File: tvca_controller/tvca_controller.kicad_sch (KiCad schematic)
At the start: 17 parts, among them J1 Programming Header, J2 Can Connector, U1 MCP2562, U2 PIC18F26K83, U5 INA180A1, Y1 Crystal

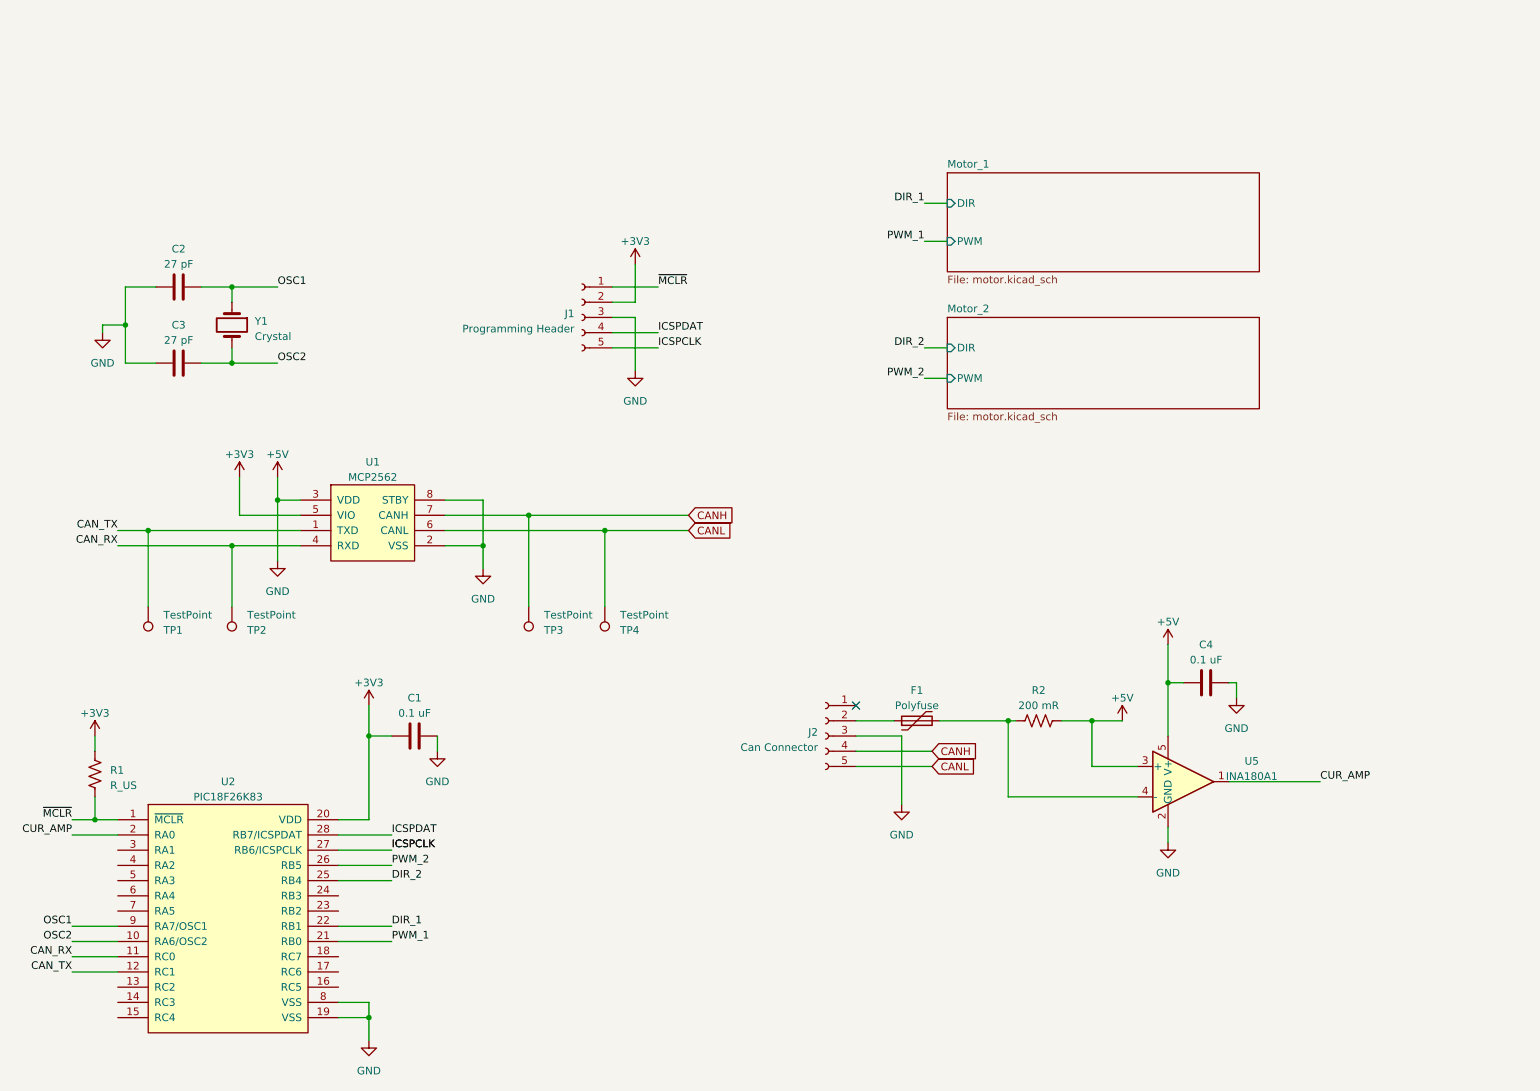
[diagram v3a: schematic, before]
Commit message: remove zips, refactor PCB to use software in place of 2-bit mux
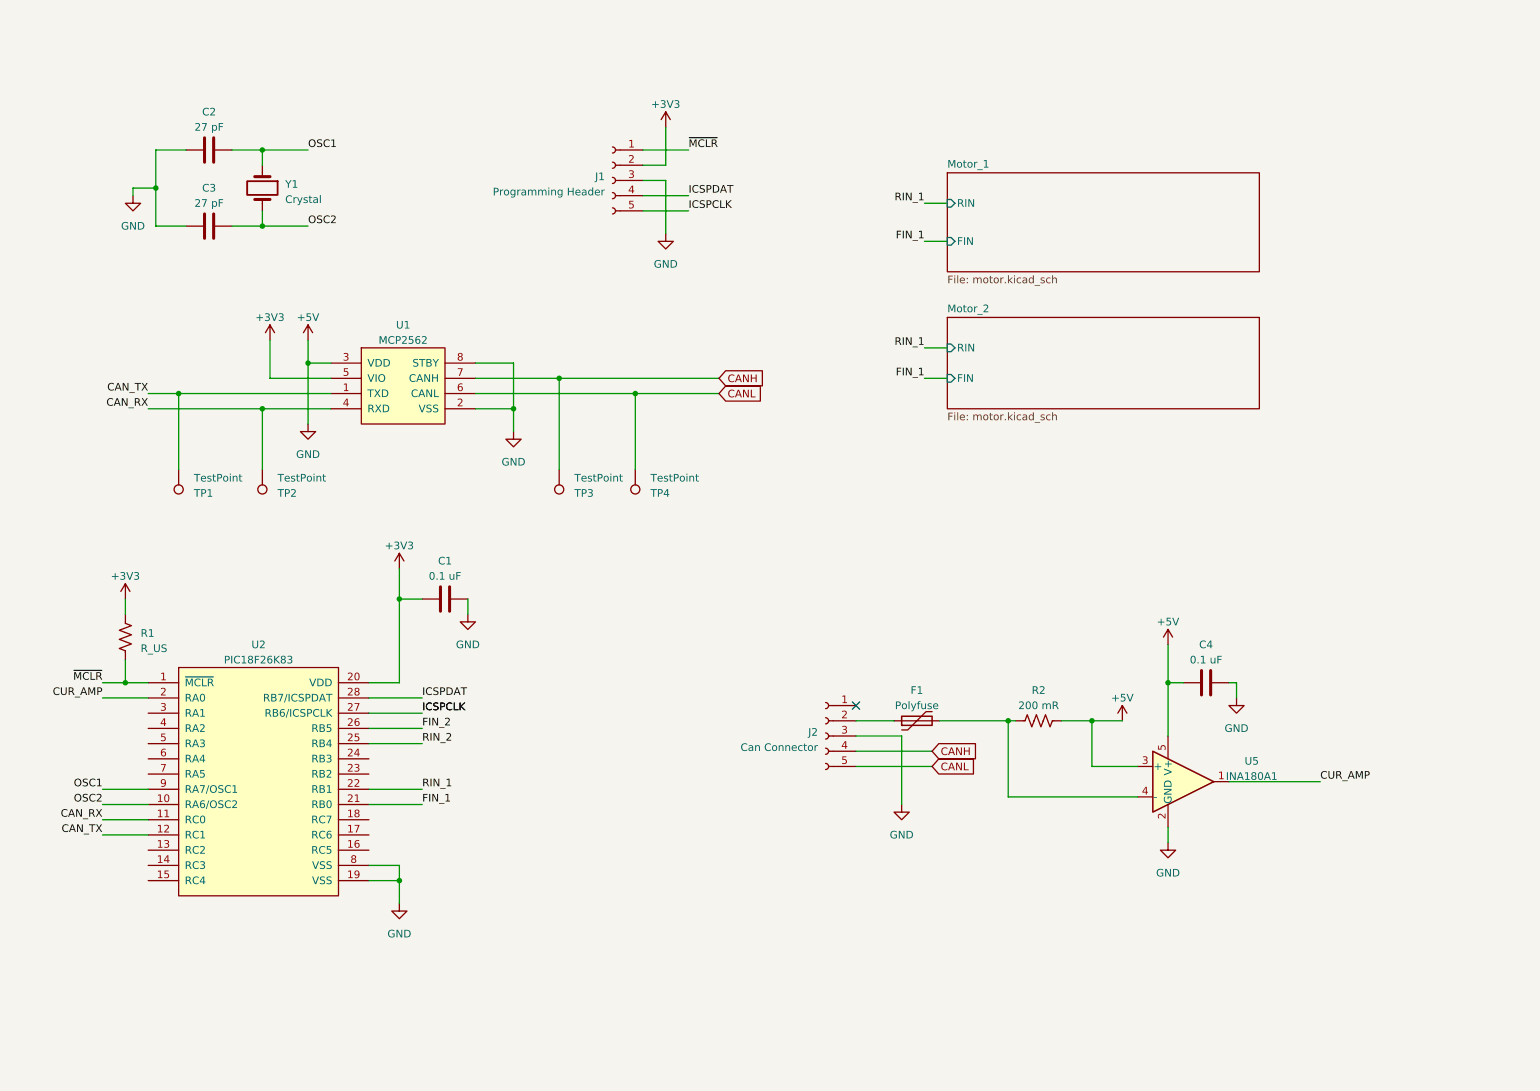
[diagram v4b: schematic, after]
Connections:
- net DIR_1 renamed RIN_1
- net DIR_2 renamed RIN_2
- net PWM_1 renamed FIN_1
- net PWM_2 renamed FIN_2
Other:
- sheet Motor_1 ports: added FIN, RIN; removed DIR, PWM
- sheet Motor_2 ports: added FIN, RIN; removed DIR, PWM
- moved on the sheet: C1, C2, C3, J1, R1, TP1, TP2, TP3, TP4, U1, U2, Y1

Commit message: add connectors
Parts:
- added J7: Batt - 12V, symbol Connector:Screw_Terminal_01x02
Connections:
- net +5V: now also J7.2 (Pin_2)
- net A_1: now reaches U2.3 (RA1)
- net B_1: now reaches U2.4 (RA2)
- net A_2: now reaches U2.5 (RA3)
- net B_2: now reaches U2.6 (RA4)
- new net BATT: J7.1 (Pin_1)
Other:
- sheet Motor_1 ports: added A, B, POW; removed none
- sheet Motor_2 ports: added A, B, POW; removed none
- note added: "PWM Input Signals"
- note added: "Quadrature Encoder Output"

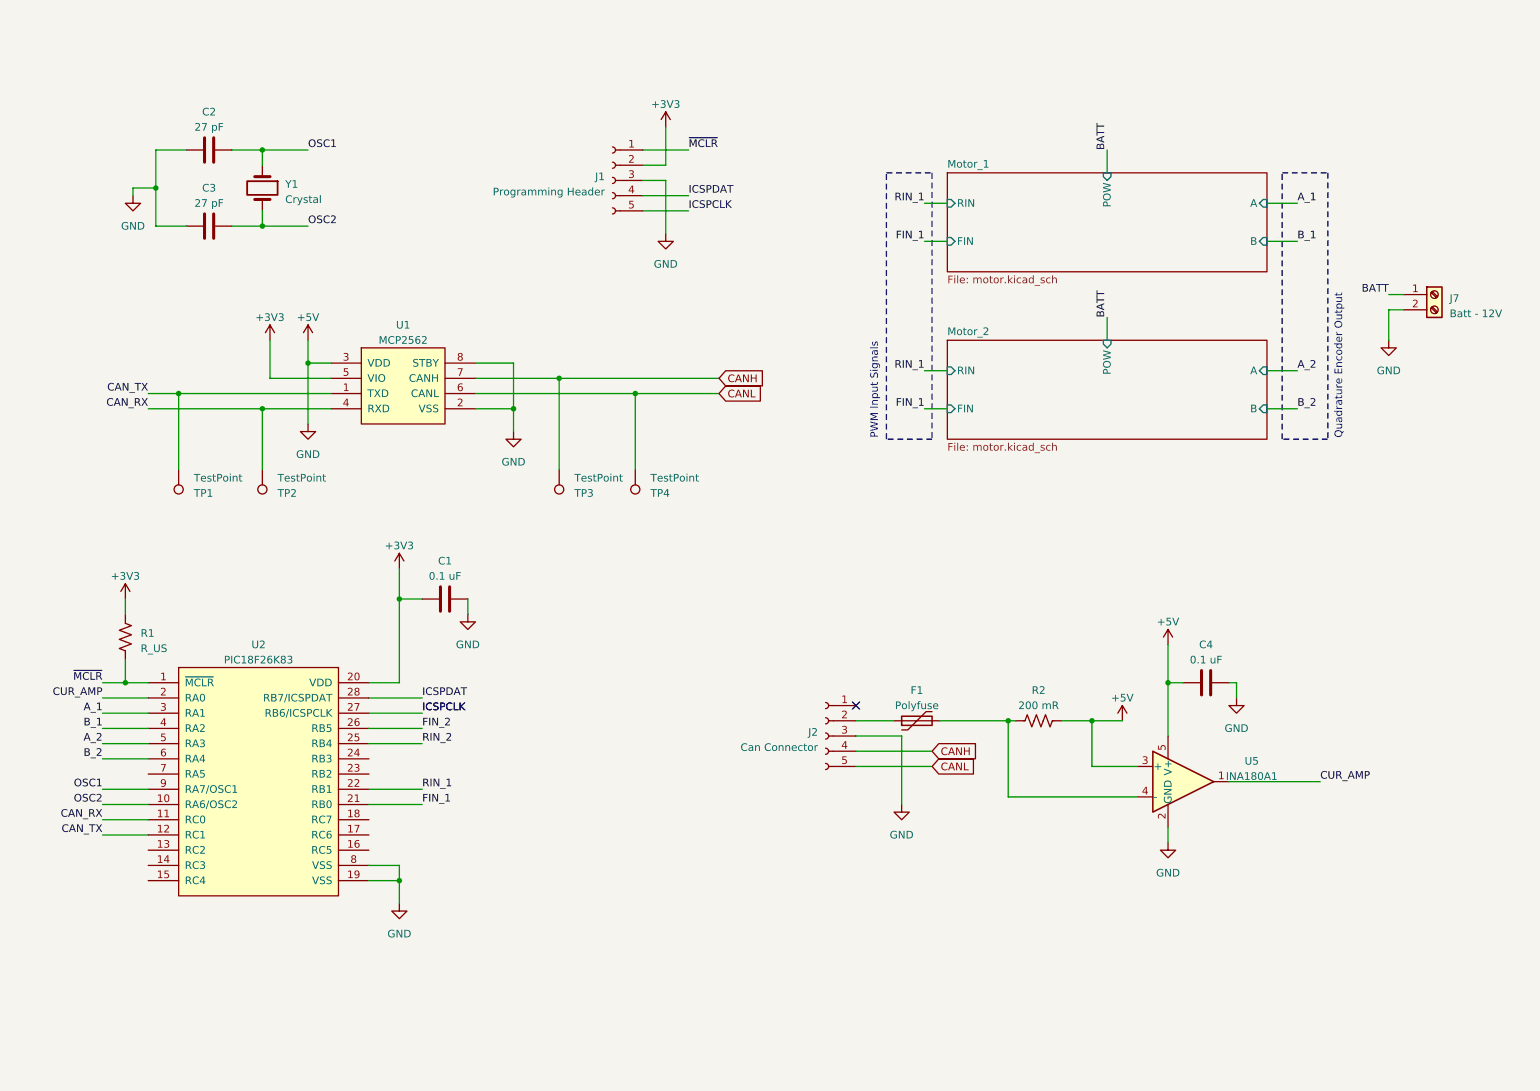
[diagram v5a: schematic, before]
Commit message: add current and voltage sensing. Address minor fixes suggested by Jack. Ready for final review
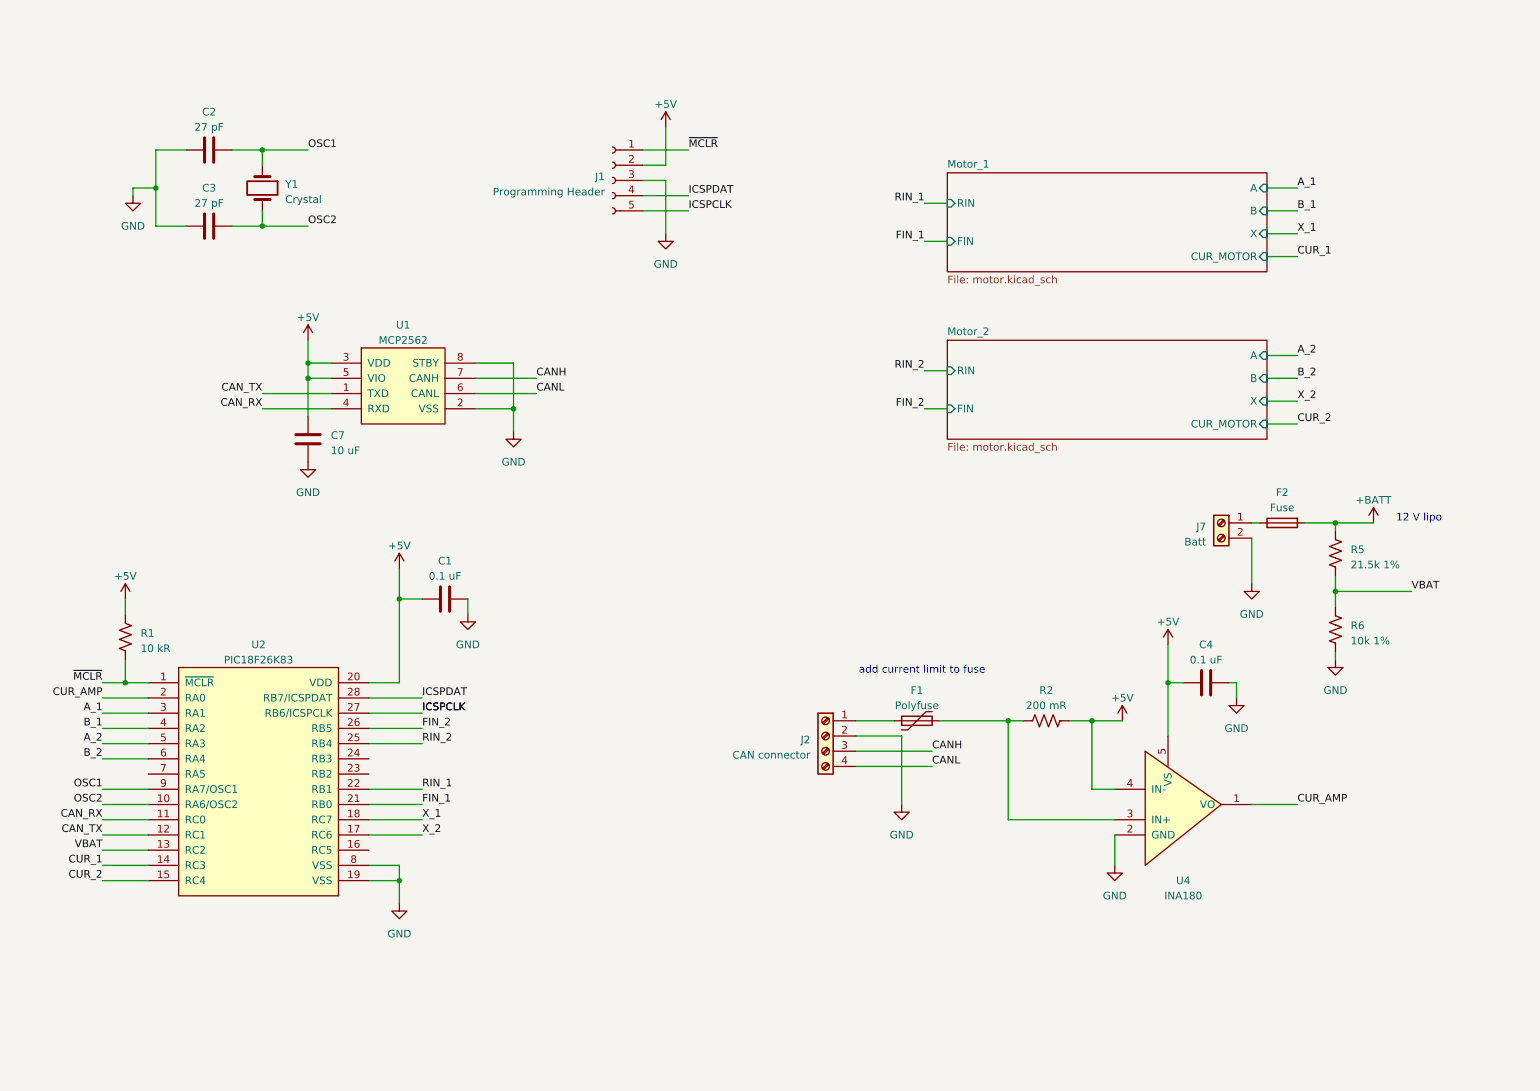
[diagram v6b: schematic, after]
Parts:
- removed J2: Can Connector, symbol Connector:Conn_01x05_Socket
- removed TP1, TP2, TP3, TP4: TestPoint, symbol Connector:TestPoint
- removed U5: INA180A1, Package_TO_SOT_SMD:SOT-23-5, symbol Amplifier_Current:INA180A1
- added C7: 10 uF, symbol Device:C
- added F2: Fuse, symbol Device:Fuse
- added J2: CAN connector, symbol Connector:Screw_Terminal_01x04
- added R5: 21.5k 1%, symbol Device:R_US
- added R6: 10k 1%, symbol Device:R_US
- added U4: INA180, symbol canhw:INA180
- J7: value Batt - 12V -> Batt
- R1: value R_US -> 10 kR
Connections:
- net +3V3 is gone; now on net +5V: C1.1, J1.2 (Pin_2), R1.1, U1.5 (VIO), U2.20 (VDD)
- net +5V: now also C7.1, U4.4 (IN-), U4.5 (VS); no longer C1.2, C2.2, C3.2, C4.2, J1.3 (Pin_3), J7.2 (Pin_2), U1.2 (VSS), U1.8 (STBY), U2.19 (VSS), U2.8 (VSS)
- net CANH: now also J2.3 (Pin_3)
- net CANL: now also J2.4 (Pin_4)
- net CUR_AMP: now also U4.1 (VO)
- net at F1.1: now also J2.1 (Pin_1)
- net at F1.2, R2.2: now also U4.3 (IN+)
- net VBAT: now reaches U2.13 (RC2)
- net VBAT: now also R5.2, R6.1
- net CUR_1: now reaches U2.14 (RC3)
- net CUR_2: now reaches U2.15 (RC4)
- net X_2: now reaches U2.17 (RC6)
- net X_1: now reaches U2.18 (RC7)
- net BATT: no longer names the net of J7.1 (Pin_1)
- net BATT: now also F2.1
- new net +BATT: F2.2, R5.1
- new net GND: C1.2, C2.2, C3.2, C4.2, C7.2, J1.3 (Pin_3), J2.2 (Pin_2), J7.2 (Pin_2), R6.2, U1.2 (VSS), U1.8 (STBY), U2.19 (VSS), U2.8 (VSS), U4.2 (GND)
- no-connect marks 1 -> 0
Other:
- sheet Motor_1 ports: added CUR_MOTOR, X; removed POW
- sheet Motor_2 ports: added CUR_MOTOR, X; removed POW
- note added: "12 V lipo"
- note added: "add current limit to fuse"
- note removed: "PWM Input Signals"
- note removed: "Quadrature Encoder Output"
- moved on the sheet: J7, R2

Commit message: Add foot prints, numerous other small changes
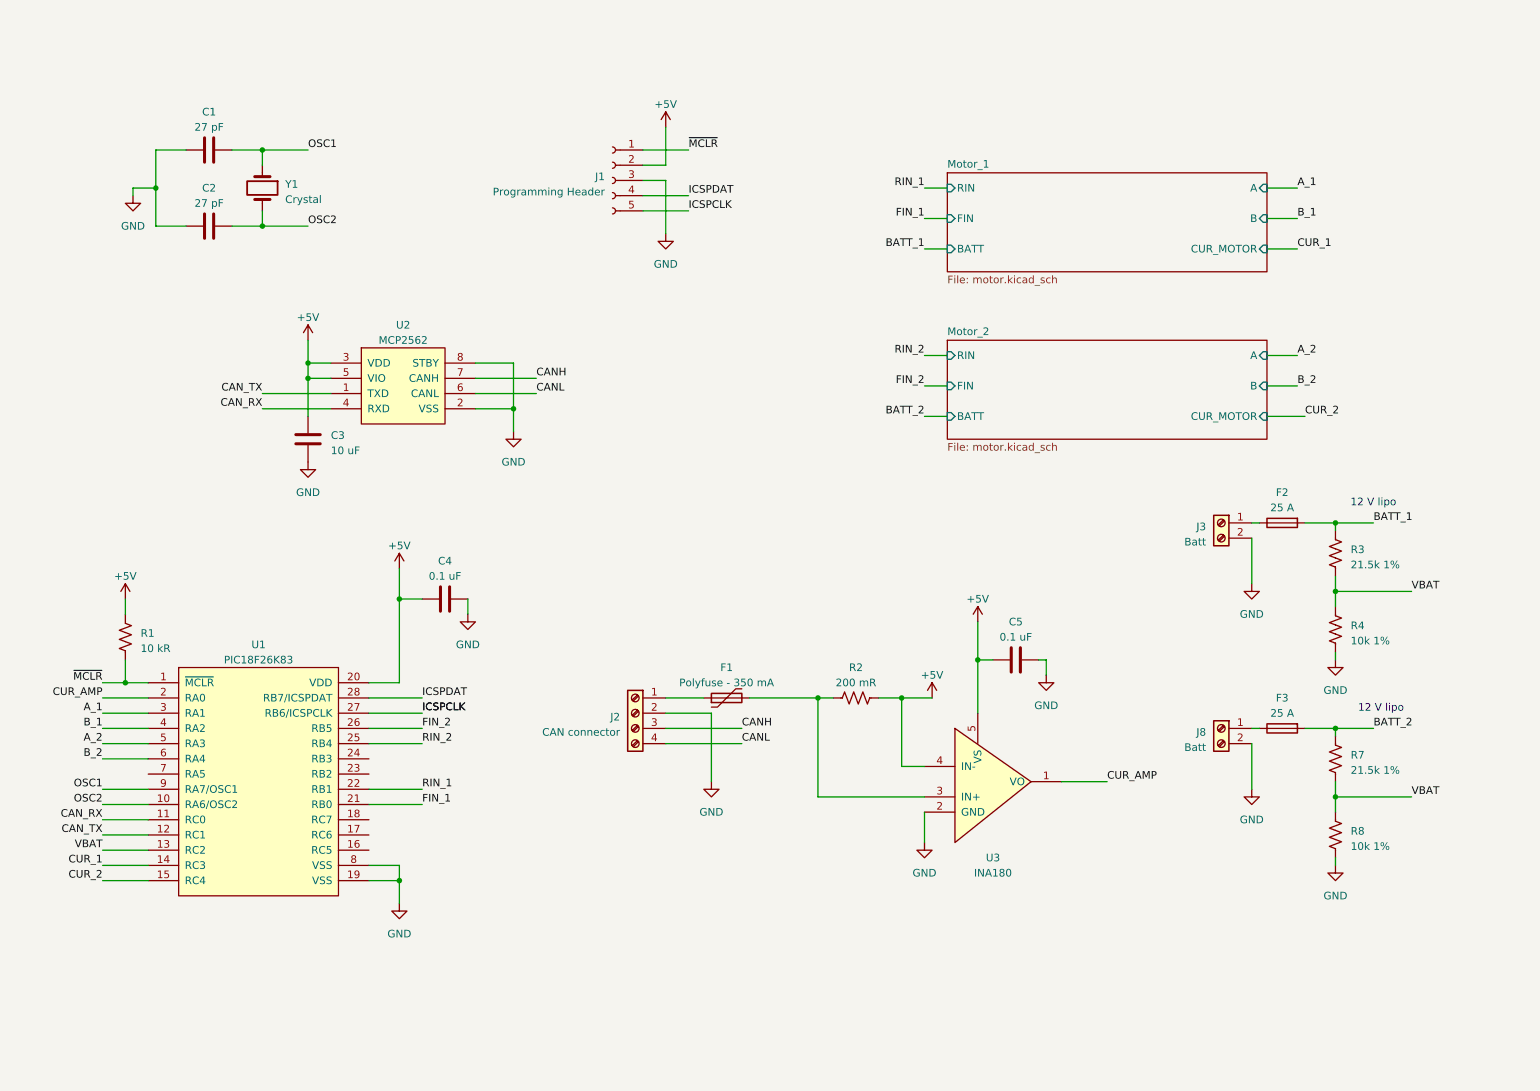
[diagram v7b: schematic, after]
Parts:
- added F3: 25 A, Fuse:Fuseholder_Cylinder-6.3x32mm_Schurter_0031-8002_Horizontal_Open, symbol Device:Fuse
- added J8: Batt, canhw_footprints:TE_2-1437667-4, symbol Connector:Screw_Terminal_01x02
- added R7: 21.5k 1%, Resistor_SMD:R_0805_2012Metric_Pad1.20x1.40mm_HandSolder, symbol Device:R_US
- added R8: 10k 1%, Resistor_SMD:R_0805_2012Metric_Pad1.20x1.40mm_HandSolder, symbol Device:R_US
- C1: renamed from C2; footprint (none) -> Capacitor_SMD:C_0805_2012Metric_Pad1.18x1.45mm_HandSolder
- C2: renamed from C3; footprint (none) -> Capacitor_SMD:C_0805_2012Metric_Pad1.18x1.45mm_HandSolder
- C3: renamed from C7; footprint (none) -> Capacitor_SMD:C_0805_2012Metric_Pad1.18x1.45mm_HandSolder
- C4: renamed from C1; footprint (none) -> Capacitor_SMD:C_0805_2012Metric_Pad1.18x1.45mm_HandSolder
- C5: renamed from C4; footprint (none) -> Capacitor_SMD:C_0805_2012Metric_Pad1.18x1.45mm_HandSolder
- F1: value Polyfuse -> Polyfuse - 350 mA; footprint (none) -> Fuse:Fuse_1206_3216Metric_Pad1.42x1.75mm_HandSolder
- F2: value Fuse -> 25 A; footprint (none) -> Fuse:Fuseholder_Cylinder-6.3x32mm_Schurter_0031-8002_Horizontal_Open
- J1: footprint (none) -> canhw_footprints:PinSocket_5x2.54_SMD_90deg_952-3198-1-ND
- J2: footprint (none) -> TerminalBlock_Phoenix:TerminalBlock_Phoenix_PT-1,5-4-5.0-H_1x04_P5.00mm_Horizontal
- J3: renamed from J7; footprint (none) -> canhw_footprints:TE_2-1437667-4
- R1, R2: footprint (none) -> Resistor_SMD:R_0805_2012Metric_Pad1.20x1.40mm_HandSolder
- R3: renamed from R5; footprint (none) -> Resistor_SMD:R_0805_2012Metric_Pad1.20x1.40mm_HandSolder
- R4: renamed from R6; footprint (none) -> Resistor_SMD:R_0805_2012Metric_Pad1.20x1.40mm_HandSolder
- U1: renamed from U2; footprint (none) -> Package_SO:SOIC-28W_7.5x18.7mm_P1.27mm
- U2: renamed from U1; footprint (none) -> Package_SO:SOIC-8_3.9x4.9mm_P1.27mm
- U3: renamed from U4; footprint (none) -> Package_TO_SOT_SMD:SOT-23-5_HandSoldering
- Y1: footprint (none) -> Crystal:Crystal_HC49-4H_Vertical
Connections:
- net GND: now also J8.2 (Pin_2), R8.2
- net VBAT: now also R7.2, R8.1
- net +BATT renamed BATT_1
- net X_1: no longer names the net of U1.18 (RC7)
- net X_2: no longer names the net of U1.17 (RC6)
- new net: F3.1, J8.1 (Pin_1)
- new net BATT_2: F3.2, R7.1
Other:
- sheet Motor_1 ports: added BATT; removed X
- sheet Motor_2 ports: added BATT; removed X
- note removed: "add current limit to fuse"
- moved on the sheet: C5, F1, J2, R2, U3
